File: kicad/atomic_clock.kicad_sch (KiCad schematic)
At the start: 80 parts, among them J1 Conn_02x05_Top_Bottom, J10 Conn_02x05_Top_Bottom, J11 Conn_02x05_Top_Bottom, J12 USB_B_Micro 10118194-0001LF, J13 ARM_JTAG_SWD_10 3220-10-0100-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, J14 Conn_01x03_Female, J2 Conn_02x05_Top_Bottom, J3 Conn_02x05_Top_Bottom, J4 Conn_02x05_Top_Bottom, J5 USB_B_Micro 1051330001, J6 Conn_02x05_Top_Bottom, J7 Conn_02x05_Top_Bottom, J8 Conn_02x05_Top_Bottom, J9 Conn_02x05_Top_Bottom, Q1 Q_Dual_PMOS, Q2 Q_Dual_PMOS, SW1 SW_Push, U1 D198K, U10 ATSAMDA1E16B-A, U11 D198K, U12 D198K, U13 D198K, U14 D198K, U15 D198K, U16 MAX7221xWG, U17 D198K, U18 D198K, U19 D198K, U2 D198K, U20 NCP1117LPST33T3G, U21 mems_osc_st1630, U22 DHT20, U23 DCF77, U24 MCP73831-2-OT, U25 TXB0101, U3 D198K, U4 D198K, U5 MAX7221xWG, U6 D198K, U7 D198K, U8 D198K, U9 D198K

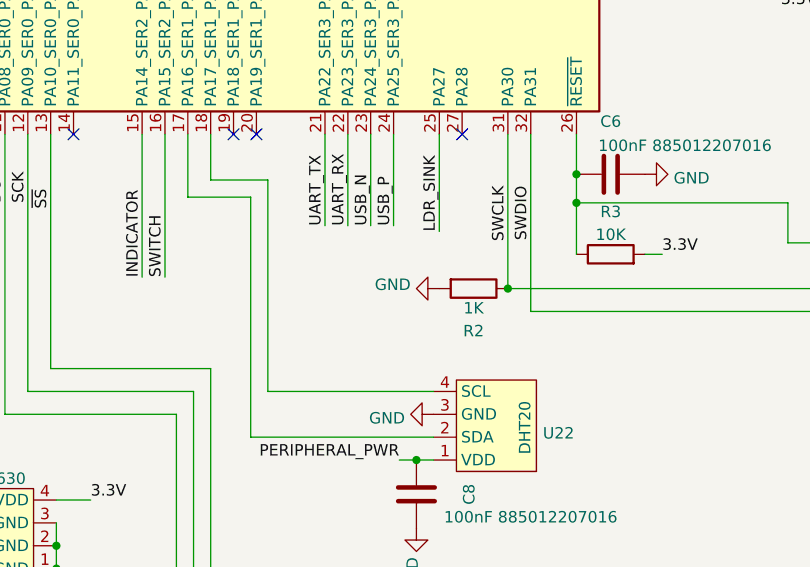
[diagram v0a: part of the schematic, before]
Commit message: Fix pull-up resistor on SWCLK
See https://twitter.com/erikvanzijst/status/1541787726684585988
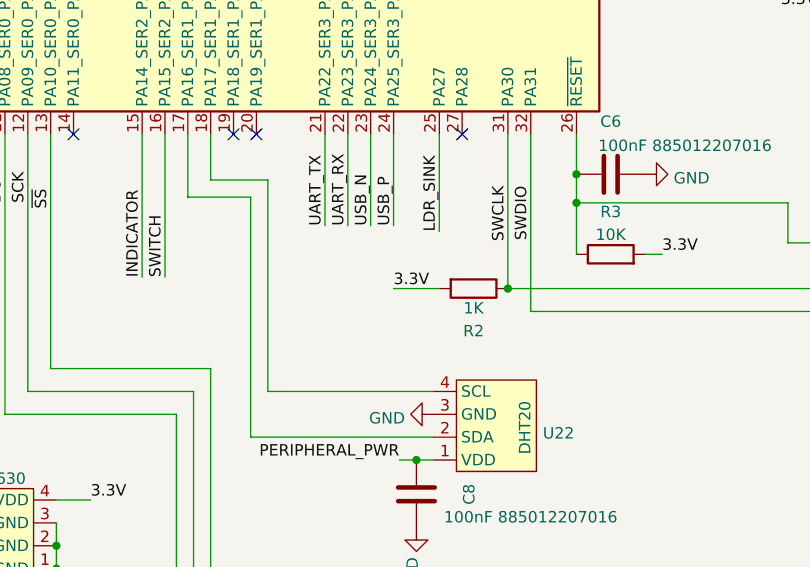
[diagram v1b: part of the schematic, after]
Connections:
- net 3.3V: now also R2.2
- net GND: no longer R2.2
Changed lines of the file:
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@@
     (stroke (width 0) (type default) (color 0 0 0 0))
   )
+  (wire (pts (xy 337.185 138.43) (xy 342.265 138.43))
+    (stroke (width 0) (type default) (color 0 0 0 0))
+  )
   (bus (pts (xy 226.695 285.75) (xy 252.095 285.75))
     (stroke (width 0) (type default) (color 0 0 0 0))
@@
     (effects (font (size 1.27 1.27)) (justify left bottom))
   )
+  (label "3.3V" (at 337.185 138.43 0)
+    (effects (font (size 1.27 1.27)) (justify left bottom))
+  )
   (label "3C2" (at 358.14 302.26 0)
     (effects (font (size 1.27 1.27)) (justify left bottom))
@@
     (pin "9")
   )
-  (symbol (lib_id "power:GND") (at 342.265 138.43 270) (unit 1)
-    (in_bom yes) (on_board yes) (fields_autoplaced)
-    (property "Reference" "#PWR0104" (id 0) (at 335.915 138.43 0)
-      (effects (font (size 1.27 1.27)) hide)
-    )
-    (property "Value" "GND" (id 1) (at 339.09 137.9962 90)
-      (effects (font (size 1.27 1.27)) (justify right))
-    )
-    (property "Footprint" "" (id 2) (at 342.265 138.43 0)
-      (effects (font (size 1.27 1.27)) hide)
-    )
-    (property "Datasheet" "" (id 3) (at 342.265 138.43 0)
-      (effects (font (size 1.27 1.27)) hide)
-    )
-    (pin "1")
-  )
   (symbol (lib_id "power:GND") (at 50.8 141.605 0) (unit 1)
     (in_bom yes) (on_board yes) (fields_autoplaced)
@@
       (reference "#PWR0103") (unit 1) (value "GND") (footprint "")
     )
-    (path "/cec0eddd-a533-4084-8214-ba2107d0c7bd"
-      (reference "#PWR0104") (unit 1) (value "GND") (footprint "")
-    )
     (path "/97c01949-0974-42e8-9648-46c689c17d81"

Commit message: Add TODO list for PCB v1.1
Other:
- note added: "TODO: * Jumper to disconnect battery * Dipswitch/jumpers for EU timezone * Redo LDR * Micro to farthest board edge * ISET resistors MAXIM * 22uF capacitor on LED"
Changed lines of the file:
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@@
     (effects (font (size 1.27 1.27)) (justify left bottom))
+  )
+  (text "TODO:\n* Jumper to disconnect battery\n* Dipswitch/jumpers for EU timezone\n* Redo LDR\n* Micro to farthest board edge\n* ISET resistors MAXIM\n* 22uF capacitor on LED"
+    (at 234.95 55.245 0)
+    (effects (font (size 3.27 3.27)) (justify left bottom))
   )
   (text "Horizontal USB connector\nPower only" (at 39.37 152.4 0)

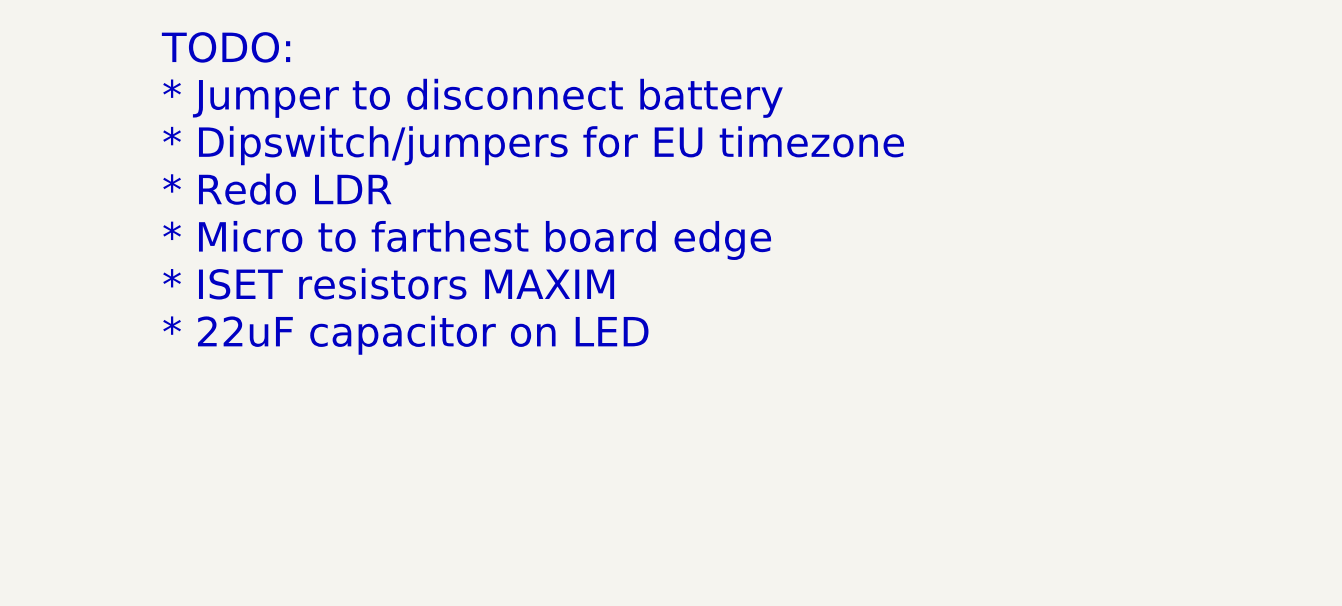
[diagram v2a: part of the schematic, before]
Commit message: Wire up USB power sense, reset button and hibernation
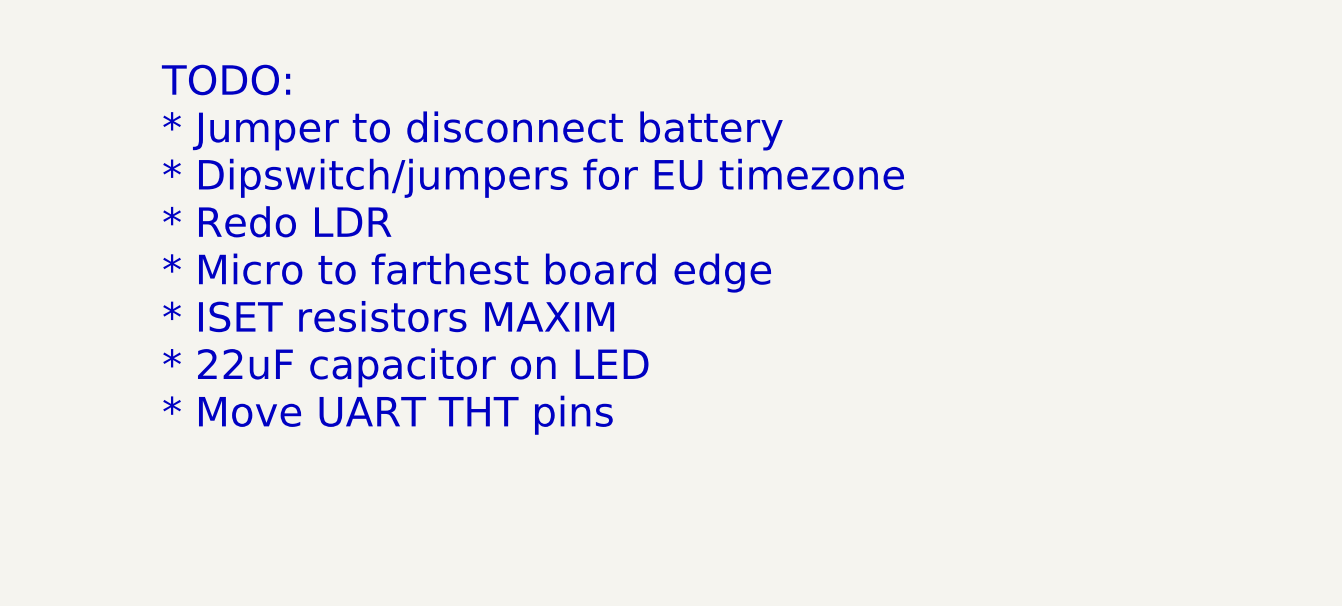
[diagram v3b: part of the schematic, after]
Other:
- note added: "TODO: * Jumper to disconnect battery * Dipswitch/jumpers for EU timezone * Redo LDR * Micro to farthest board edge * ISET resistors MAXIM * 22uF capacitor on LED * Move UART THT pins"
- note removed: "TODO: * Jumper to disconnect battery * Dipswitch/jumpers for EU timezone * Redo LDR * Micro to farthest board edge * ISET resistors MAXIM * 22uF capacitor on LED"
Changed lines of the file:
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@@
     (effects (font (size 1.27 1.27)) (justify left bottom))
   )
-  (text "TODO:\n* Jumper to disconnect battery\n* Dipswitch/jumpers for EU timezone\n* Redo LDR\n* Micro to farthest board edge\n* ISET resistors MAXIM\n* 22uF capacitor on LED"
-    (at 234.95 55.245 0)
+  (text "TODO:\n* Jumper to disconnect battery\n* Dipswitch/jumpers for EU timezone\n* Redo LDR\n* Micro to farthest board edge\n* ISET resistors MAXIM\n* 22uF capacitor on LED\n* Move UART THT pins"
+    (at 234.95 64.135 0)
     (effects (font (size 3.27 3.27)) (justify left bottom))
   )

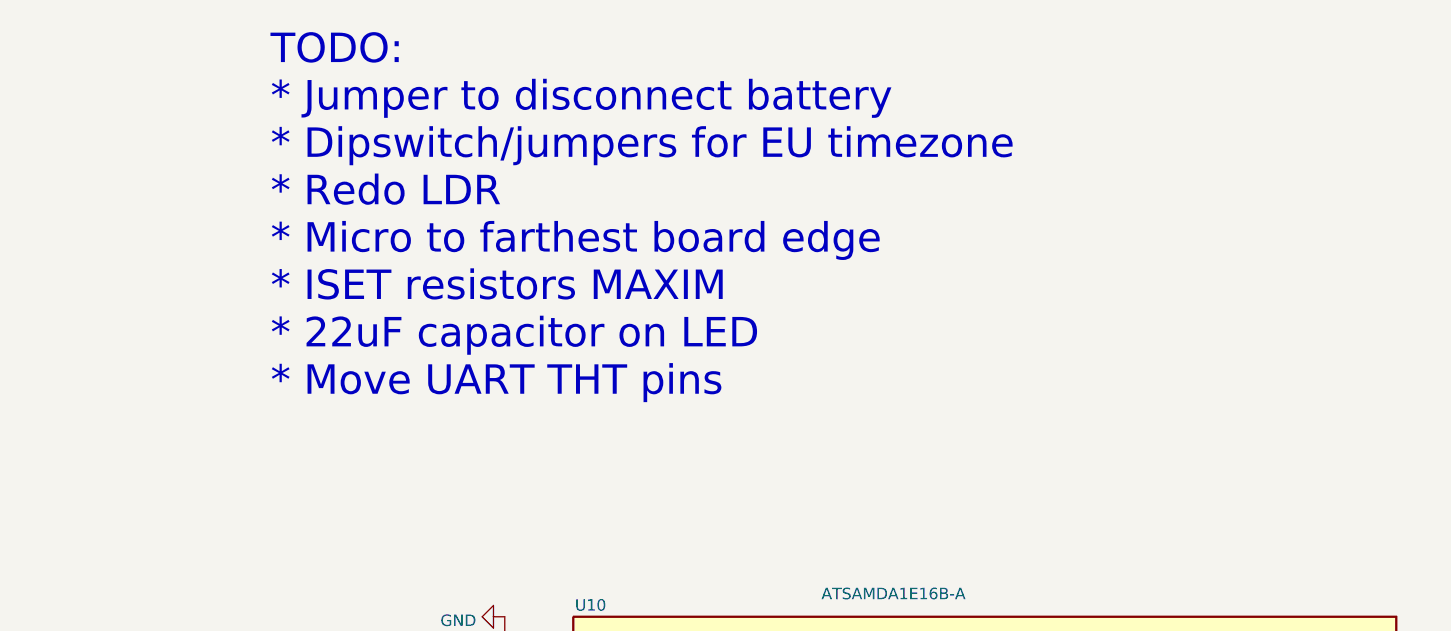
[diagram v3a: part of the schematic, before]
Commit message: Add TODO for next PCB revision
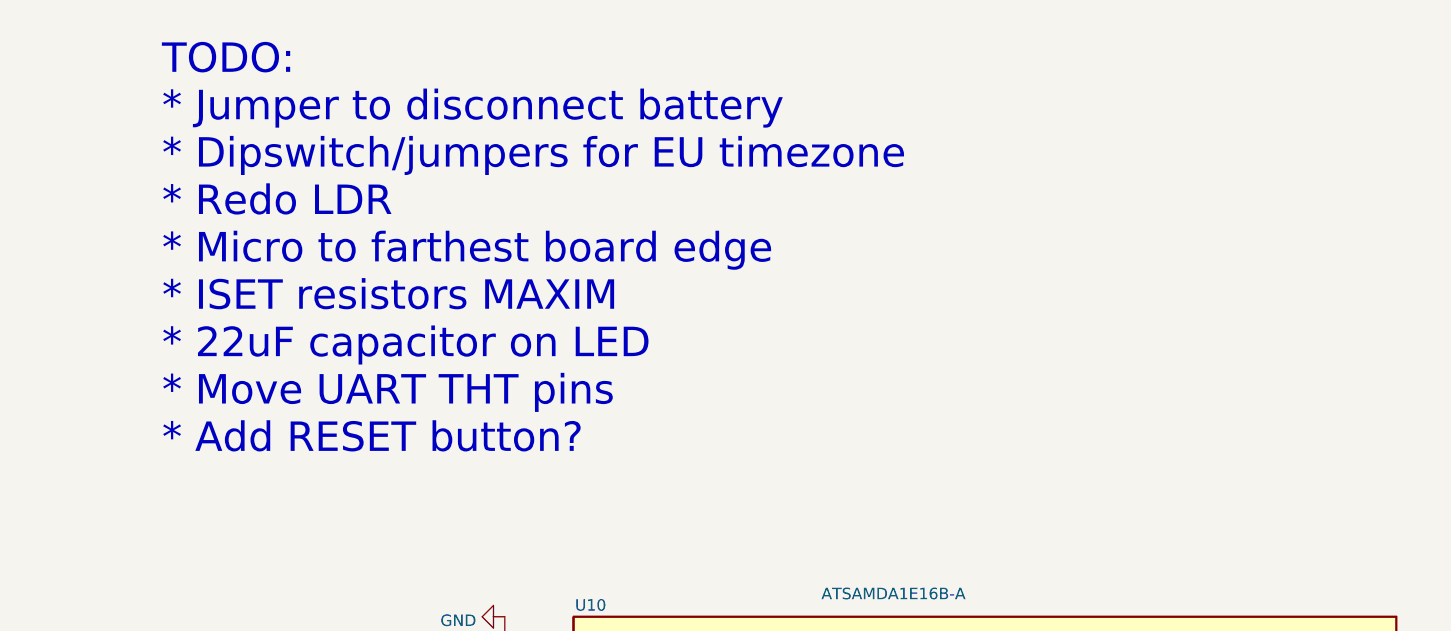
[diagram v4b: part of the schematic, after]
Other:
- note added: "TODO: * Jumper to disconnect battery * Dipswitch/jumpers for EU timezone * Redo LDR * Micro to farthest board edge * ISET resistors MAXIM * 22uF capacitor on LED * Move UART THT pins * Add RESET button?"
- note removed: "TODO: * Jumper to disconnect battery * Dipswitch/jumpers for EU timezone * Redo LDR * Micro to farthest board edge * ISET resistors MAXIM * 22uF capacitor on LED * Move UART THT pins"
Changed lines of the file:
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@@
     (effects (font (size 1.27 1.27)) (justify left bottom))
   )
-  (text "TODO:\n* Jumper to disconnect battery\n* Dipswitch/jumpers for EU timezone\n* Redo LDR\n* Micro to farthest board edge\n* ISET resistors MAXIM\n* 22uF capacitor on LED\n* Move UART THT pins"
-    (at 234.95 64.135 0)
+  (text "TODO:\n* Jumper to disconnect battery\n* Dipswitch/jumpers for EU timezone\n* Redo LDR\n* Micro to farthest board edge\n* ISET resistors MAXIM\n* 22uF capacitor on LED\n* Move UART THT pins\n* Add RESET button?"
+    (at 222.885 70.485 0)
     (effects (font (size 3.27 3.27)) (justify left bottom))
   )

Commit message: Start routing v2
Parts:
- removed D5, D6, D9: Diode S1M-13-F, Diode_SMD:D_SMA, symbol Device:D
- added J14: Conn_01x02_Male, Connector_PinHeader_2.54mm:PinHeader_1x02_P2.54mm_Vertical, symbol Connector:Conn_01x02_Male
- added J16: Conn_01x03_Male, symbol Connector:Conn_01x03_Male
- added unit 2 of Q2
- added RV1: 50K, Potentiometer_SMD:Potentiometer_Bourns_TC33X_Vertical, symbol Device:R_Potentiometer_Trim
- added SW2: SW_Push, Button_Switch_SMD:SW_SPST_TL3342, symbol Switch:SW_Push
- D8: value Diode S1M-13-F -> Schottky NSR05T40; footprint Diode_SMD:D_SMA -> Diode_SMD:D_SOD-523; Price 0.213 -> 0.283
- R5: value 10K -> 10M
- renumbered J14 to J15
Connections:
- net 3.3V: now also J16.2 (Pin_2); no longer R5.1
- net 5V: now also R5.1, R6.2; no longer R1.2, R4.2
- net GND: now also Q2.5 (G), SW2.1
- net NCP_IN: now also Q2.3 (D)
- net USB_PWR: now also J12.1 (VBUS), J5.1 (VBUS)
- net at C10.2, U24.3 (VBAT): now also J14.2 (Pin_2), Q2.4 (S); no longer BT1.1 (+)
- net ~{RESET}: now reaches C6.1, J13.10 (~{RESET}), R3.1, U10.26 (~{RESET})
- net ~{RESET}: now also SW2.2
- net TZ1: now reaches U10.19 (PA18_SER1_PAD2/SER3_PAD2)
- net TZ1: now also J16.3 (Pin_3)
- net TZ2: now reaches U10.20 (PA19_SER1_PAD3/SER3_PAD3)
- net TZ2: now also J16.1 (Pin_1)
- removed net LDR: R5.2, R6.2, U10.3 (PA02)
- net LDR_SINK: no longer names the net of R6.1
- net LDR_SINK: now also R5.2, RV1.1; no longer U10.25 (PA27)
- new net: BT1.1 (+), J14.1 (Pin_1)
- new net I_SET: R1.2, R4.2, RV1.2
- no-connect marks 37 -> 38
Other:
- note added: "TODO: * Micro to farthest board edge * 22uF capacitor on LED * Move UART THT pins * Flip DCF module upside down"
- note added: "Timezone WET (LON) - jumper on 0-1 CET (AMS) - no jumper EET (HEL) - jumper on 1-2"
- note removed: "TODO: * Jumper to disconnect battery * Dipswitch/jumpers for EU timezone * Redo LDR * Micro to farthest board edge * ISET resistors MAXIM * 22uF capacitor on LED * Move UART THT pins * Add RESET button?"
- moved on the sheet: BT1, D10, R16
